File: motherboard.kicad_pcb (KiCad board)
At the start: 2 copper layers, 90.2 x 95.9 mm, 110 parts, among them P1 CONN_02X08, U1 STM32F411-LQFP64, U10 74LS125, U11 74LS125, U12 74LS125, U13 74LS125, U14 PCA9517A, U15 PCA9517A, U16 74LS125, U17 74LS125, U2 STM32F411-LQFP64, U3 AP7313, U4 74LS00, U5 74LS125, U6 FM25V20A-G, U7 FM25V20A-G, U8 FM25V20A-G, U9 FM25V20A-G, Y1 32k, Y2 8M(16pF), Y3 32k, Y4 8M(16pF)

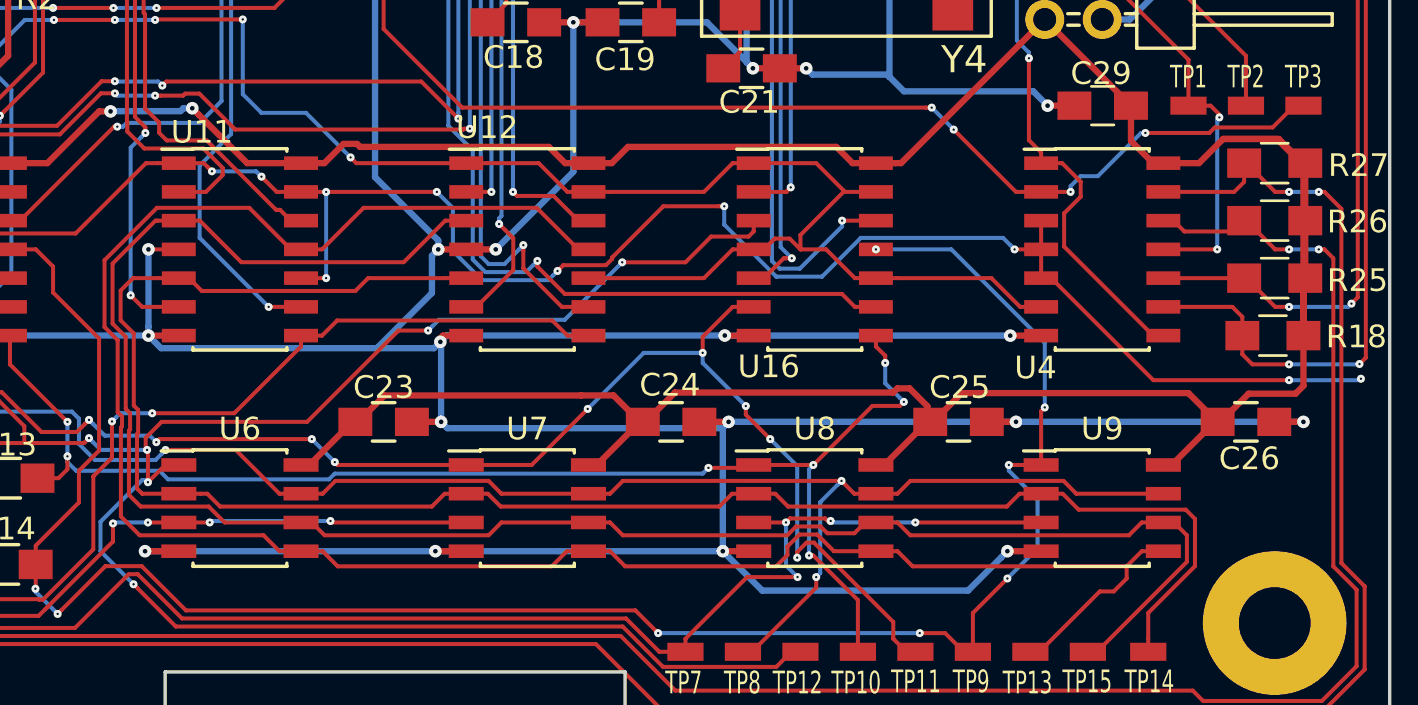
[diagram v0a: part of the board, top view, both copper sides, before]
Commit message: Adding ground plane
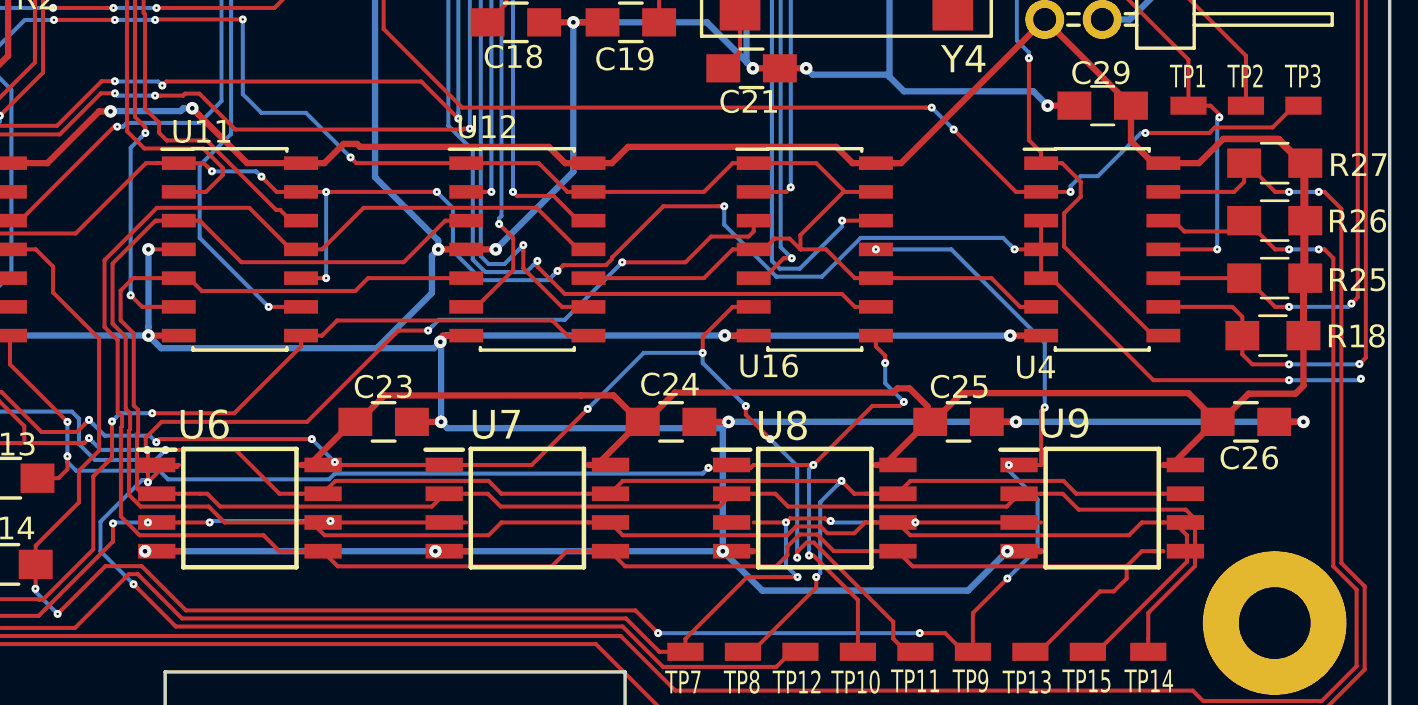
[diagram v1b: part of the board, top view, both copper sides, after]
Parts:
- U6, U7, U8, U9: footprint Housings_SOIC:SOIC-8_3.9x4.9mm_Pitch1.27mm -> FM25V20A-G:SOIC127P800X203-8N
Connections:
- C33 pad 1: /NBUFEN_SEC -> Net-(C33-Pad1)
- C33 pad 2: GND -> Net-(C33-Pad2)
- C35 pad 1: /NBUFEN_SEC -> Net-(C35-Pad1)
- C35 pad 2: GND -> Net-(C35-Pad2)
- R18 pad 2: +3V3 -> GND
- R25 pad 2: +3V3 -> GND
- R26 pad 2: +3V3 -> GND
- R27 pad 2: +3V3 -> GND
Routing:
- net /MEM_CS2: track 77.2 -> 49.7 mm, vias 9 -> 5
- net GND: track 752.4 -> 779.8 mm
- net /MEM_SCK: track 84.8 -> 111.2 mm, vias 0 -> 4
- net /MEM_NWP: track 113.3 -> 94.4 mm, vias 11 -> 7
- net /MEM_MISO: track 80.5 -> 73.1 mm
- net /NBUFEN_SEC: track 242.1 -> 235.4 mm
- net Net-(C35-Pad1): track 0.00 -> 5.90 mm
- net +3V3: track 584.4 -> 582.1 mm, vias 25 -> 29
- net Net-(C33-Pad2): track 0.00 -> 1.31 mm
- net Net-(C35-Pad2): track 0.00 -> 1.14 mm
- net Net-(C33-Pad1): track 0.00 -> 0.80 mm

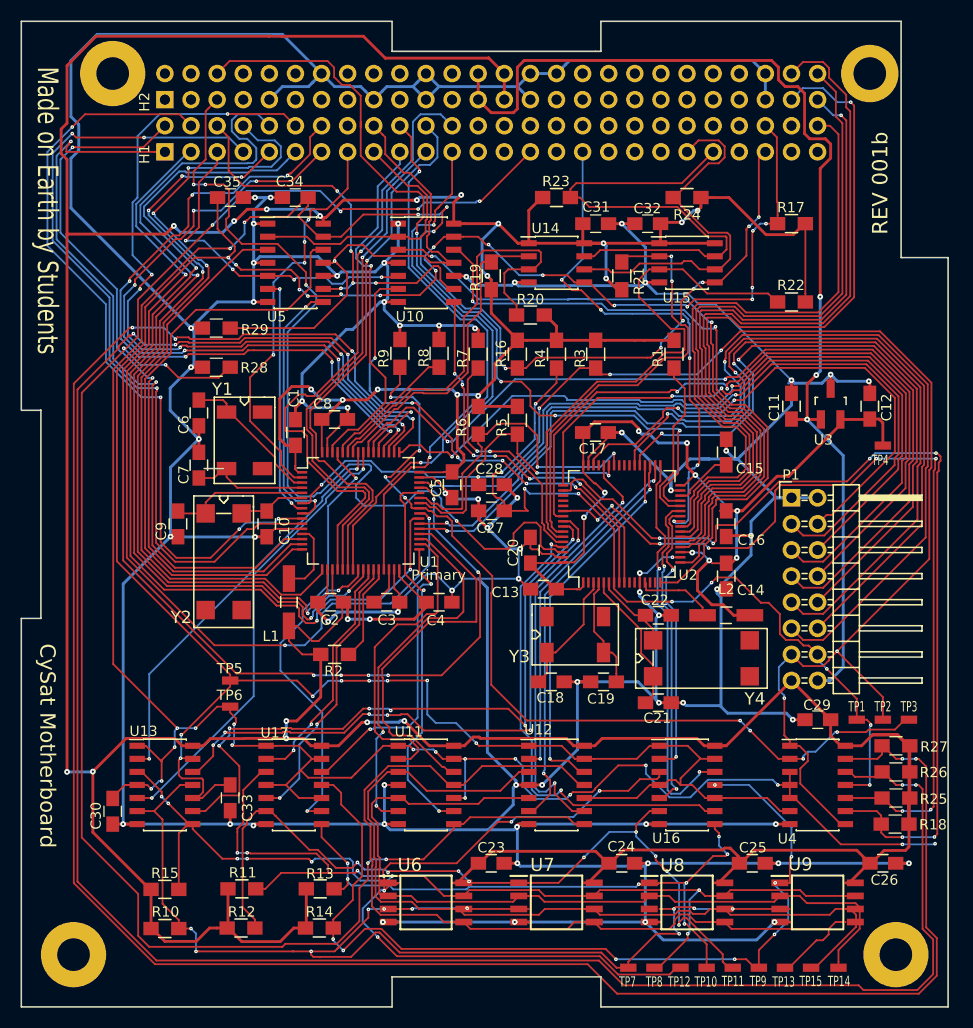
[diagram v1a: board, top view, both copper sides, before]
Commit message: Added ground plane and fixed footprints
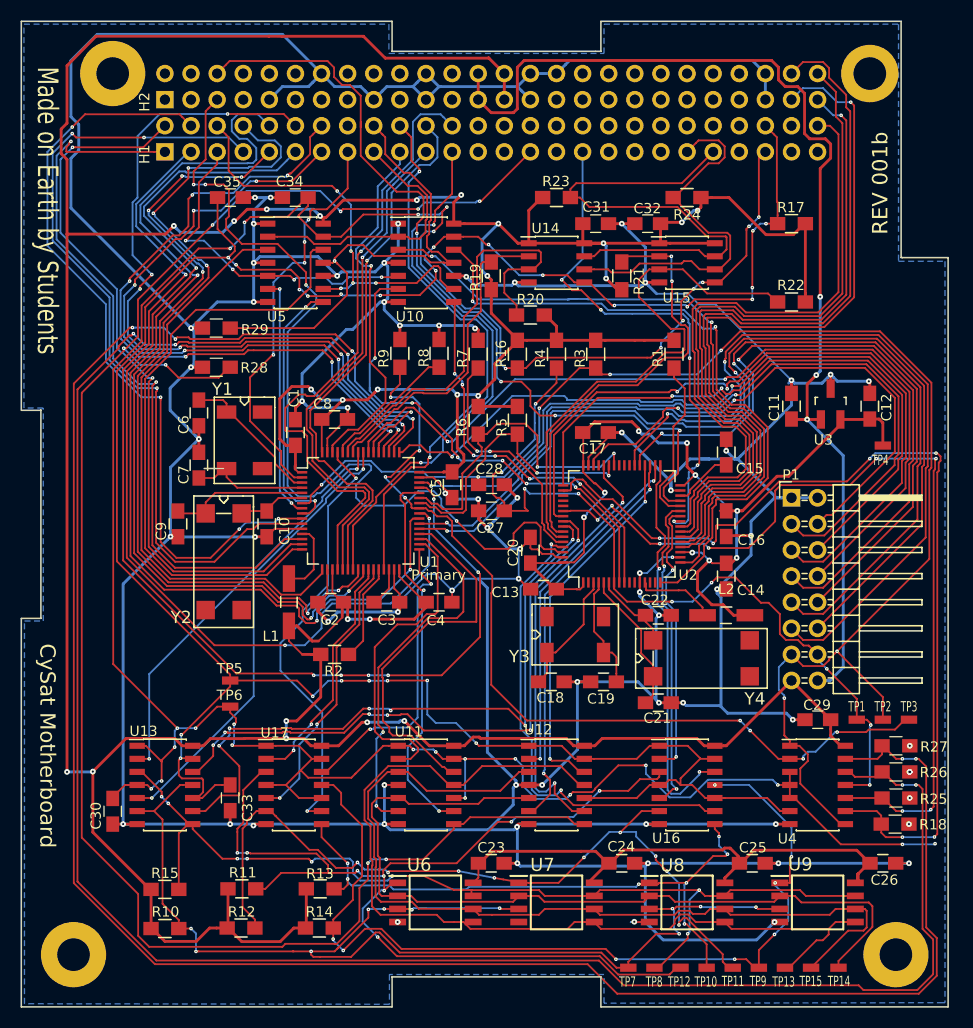
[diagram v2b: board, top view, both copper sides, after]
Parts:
- moved U6 0.91 mm to (153.3, 132.1)
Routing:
- net GND: track 779.8 -> 725.5 mm, vias 66 -> 70
- net +3V3: track 582.1 -> 549.7 mm, vias 29 -> 25
- net /MEM_CS2: track 49.7 -> 78.2 mm, vias 5 -> 9
- net /MEM_SCK: track 111.2 -> 87.1 mm, vias 4 -> 0
- net /MEM_NWP: track 94.4 -> 112.5 mm, vias 7 -> 11
- net /MEM_MISO: track 73.1 -> 82.3 mm
- net /MEM_CS1: track 60.2 -> 61.2 mm
- net /MEM_MOSI: track 92.4 -> 93.4 mm
- added copper zone on B.Cu, net GND

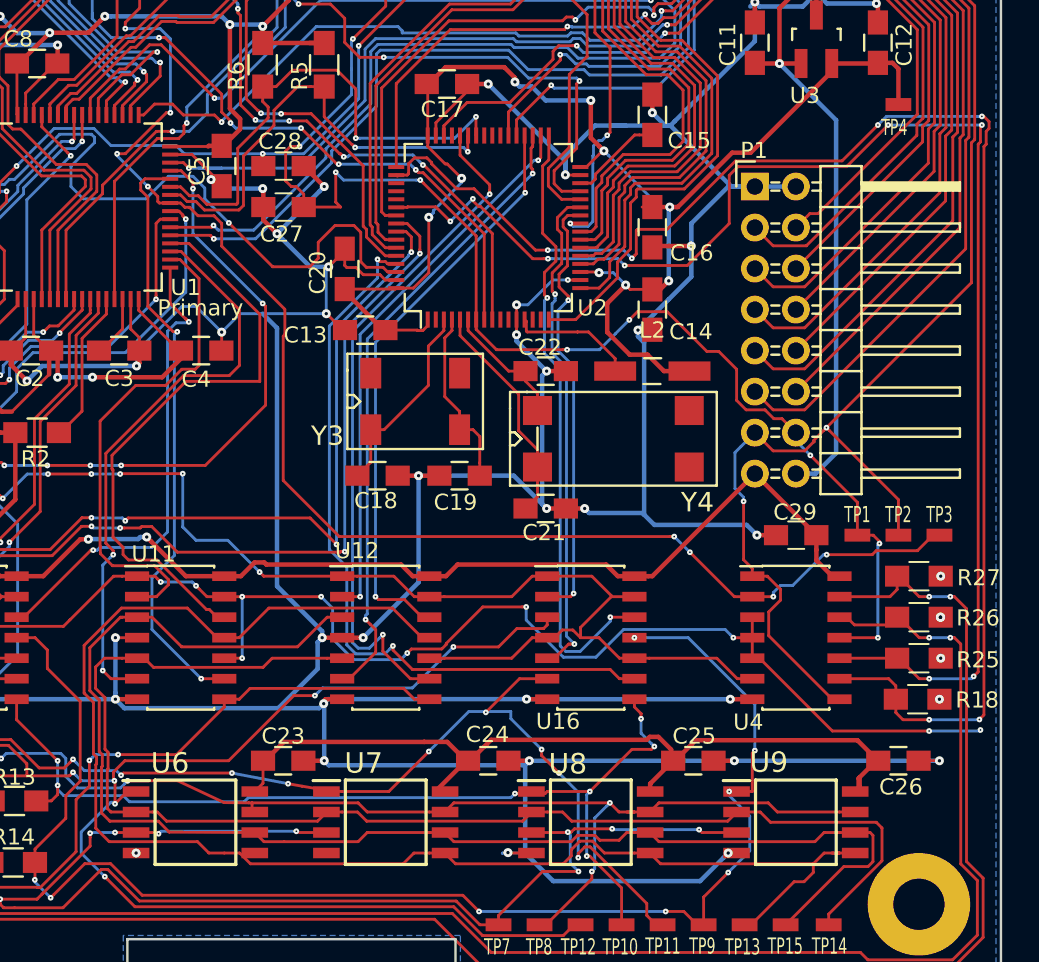
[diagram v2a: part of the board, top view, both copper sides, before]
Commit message: Added ground plane and fixed footprints
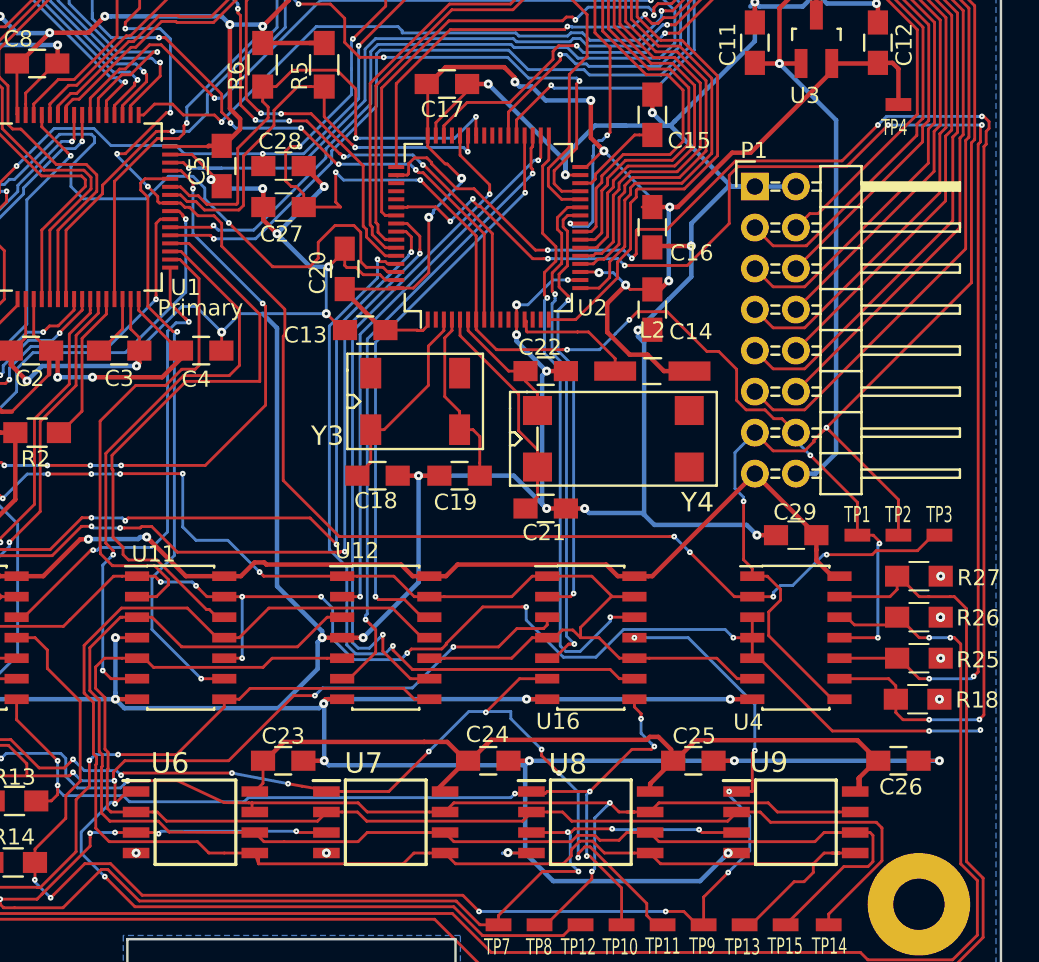
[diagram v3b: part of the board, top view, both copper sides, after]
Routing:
- net /MEM_MOSI: track 93.4 -> 94.4 mm
- net GND: vias 70 -> 71
- net /NRST2_S: vias 6 -> 4
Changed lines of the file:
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@@
   (general
     (links 392)
-    (no_connects 15)
+    (no_connects 13)
     (area 110.878219 46.279999 205.351781 142.315001)
     (thickness 1.6)
     (drawings 25)
-    (tracks 4148)
+    (tracks 4153)
     (zones 0)
     (modules 110)
@@
   (layers
     (0 F.Cu signal)
-    (31 B.Cu signal hide)
+    (31 B.Cu signal)
     (32 B.Adhes user hide)
     (33 F.Adhes user hide)
@@
       (effects (font (size 1 1) (thickness 0.15)))
     )
-    (pad 1 thru_hole circle (at 0 0) (size 6.35 6.35) (drill 3.175) (layers *.Mask B.Cu))
+    (pad 1 thru_hole circle (at 0 0) (size 6.35 6.35) (drill 3.175) (layers *.Cu *.Mask))
   )
   (module motherboard:Hole_0.125-0.250 locked (layer F.Cu)
@@
   (gr_line (start 149.098 139.319) (end 169.418 139.319) (layer Edge.Cuts) (width 0.15))
   (gr_line (start 149.098 142.24) (end 149.098 139.319) (layer Edge.Cuts) (width 0.15))
-  (via (at 199.47 116.84) (size 0.5588) (drill 0.2032) (layers F.Cu B.Cu) (net 1) (status C00000))
+  (via (at 161.425 133.985) (size 0.5588) (drill 0.2032) (layers F.Cu B.Cu) (net 1))
+  (segment (start 161.4424 134.0104) (end 161.4424 134.0024) (width 0.1778) (layer B.Cu) (net 1))
+  (segment (start 161.4424 134.0024) (end 161.425 133.985) (width 0.1778) (layer B.Cu) (net 1))
+  (via (at 199.47 116.84) (size 0.5588) (drill 0.2032) (layers F.Cu B.Cu) (net 1))
   (segment (start 199.37 116.84) (end 199.47 116.84) (width 0.2794) (layer F.Cu) (net 1))
-  (segment (start 199.47 116.84) (end 199.4408 116.84) (width 0.1778) (layer B.Cu) (net 1) (status 400000))
-  (via (at 199.47 119.38) (size 0.5588) (drill 0.2032) (layers F.Cu B.Cu) (net 1) (status C00000))
-  (segment (start 199.4408 119.38) (end 199.47 119.38) (width 0.1778) (layer F.Cu) (net 1) (status C00000))
-  (via (at 199.4408 119.38) (size 0.5588) (drill 0.2032) (layers F.Cu B.Cu) (net 1) (status 800000))
-  (segment (start 199.47 119.38) (end 199.4408 119.38) (width 0.1778) (layer B.Cu) (net 1) (status 400000))
-  (via (at 199.39 124.46) (size 0.5588) (drill 0.2032) (layers F.Cu B.Cu) (net 1) (status C00000))
-  (via (at 199.47 121.92) (size 0.5588) (drill 0.2032) (layers F.Cu B.Cu) (net 1) (status C00000))
+  (segment (start 199.47 116.84) (end 199.4408 116.84) (width 0.1778) (layer B.Cu) (net 1))
+  (via (at 199.47 119.38) (size 0.5588) (drill 0.2032) (layers F.Cu B.Cu) (net 1))
+  (segment (start 199.4408 119.38) (end 199.47 119.38) (width 0.1778) (layer F.Cu) (net 1))
+  (via (at 199.4408 119.38) (size 0.5588) (drill 0.2032) (layers F.Cu B.Cu) (net 1))
+  (segment (start 199.47 119.38) (end 199.4408 119.38) (width 0.1778) (layer B.Cu) (net 1))
+  (via (at 199.39 124.46) (size 0.5588) (drill 0.2032) (layers F.Cu B.Cu) (net 1))
+  (via (at 199.47 121.92) (size 0.5588) (drill 0.2032) (layers F.Cu B.Cu) (net 1))
   (segment (start 199.39 122) (end 199.47 121.92) (width 0.2794) (layer F.Cu) (net 1))
-  (segment (start 199.47 121.92) (end 199.4408 121.92) (width 0.1778) (layer B.Cu) (net 1) (status 400000))
-  (segment (start 199.3392 128.27) (end 198.1 128.27) (width 0.1778) (layer F.Cu) (net 1) (status 800000))
-  (segment (start 174.125 133.985) (end 172.6946 133.985) (width 0.1778) (layer F.Cu) (net 1) (status 400000))
+  (segment (start 199.47 121.92) (end 199.4408 121.92) (width 0.1778) (layer B.Cu) (net 1))
+  (segment (start 199.3392 128.27) (end 198.1 128.27) (width 0.1778) (layer F.Cu) (net 1))
+  (segment (start 174.125 133.985) (end 172.6946 133.985) (width 0.1778) (layer F.Cu) (net 1))
   (via (at 172.6692 133.9596) (size 0.5588) (drill 0.2032) (layers F.Cu B.Cu) (net 1))
   (segment (start 172.6946 133.985) (end 172.6692 133.9596) (width 0.1778) (layer F.Cu) (net 1))
@@
   (segment (start 172.6692 133.985) (end 172.339 133.985) (width 0.1778) (layer B.Cu) (net 1))
   (segment (start 172.339 133.985) (end 172.3136 134.0104) (width 0.1778) (layer B.Cu) (net 1))
-  (via (at 149.6394 133.985) (size 0.5588) (drill 0.2032) (layers F.Cu B.Cu) (net 1) (status C00000))
+  (via (at 149.6394 133.985) (size 0.5588) (drill 0.2032) (layers F.Cu B.Cu) (net 1))
   (segment (start 149.2504 134.0104) (end 149.2584 134.0024) (width 0.1778) (layer B.Cu) (net 1))
   (segment (start 149.6568 134.0024) (end 149.2584 134.0024) (width 0.1778) (layer B.Cu) (net 1))
-  (segment (start 149.6568 134.0024) (end 149.6394 133.985) (width 0.1778) (layer B.Cu) (net 1) (status 800000))
+  (segment (start 149.6568 134.0024) (end 149.6394 133.985) (width 0.1778) (layer B.Cu) (net 1))
   (segment (start 185.42 128.3208) (end 186.6392 128.3208) (width 0.1778) (layer B.Cu) (net 1))
   (segment (start 186.6392 128.3208) (end 186.69 128.27) (width 0.1778) (layer B.Cu) (net 1))
@@
   (segment (start 193.675 131.445) (end 193.2 131.445) (width 0.1778) (layer F.Cu) (net 61))
   (segment (start 180.025 131.445) (end 180.5 131.445) (width 0.1778) (layer F.Cu) (net 61))
+  (segment (start 157.226 134.653301) (end 157.226 134.2216) (width 0.1778) (layer F.Cu) (net 62))
+  (segment (start 157.226 134.2216) (end 156.9894 133.985) (width 0.1778) (layer F.Cu) (net 62))
   (segment (start 193.1416 133.985) (end 194.175 133.985) (width 0.1778) (layer F.Cu) (net 62))
   (segment (start 147.973063 133.281701) (end 153.443901 133.281701) (width 0.1778) (layer F.Cu) (net 62))
@@
   (segment (start 169.421101 134.653301) (end 168.7528 133.985) (width 0.1778) (layer F.Cu) (net 62))
   (segment (start 168.7528 133.985) (end 167.8 133.985) (width 0.1778) (layer F.Cu) (net 62))
-  (segment (start 156.0528 133.985) (end 155.1 133.985) (width 0.1778) (layer F.Cu) (net 62))
-  (segment (start 156.721101 134.653301) (end 156.0528 133.985) (width 0.1778) (layer F.Cu) (net 62))
-  (segment (start 166.178899 134.653301) (end 156.721101 134.653301) (width 0.1778) (layer F.Cu) (net 62))
+  (segment (start 156.9894 133.985) (end 155.1 133.985) (width 0.1778) (layer F.Cu) (net 62))
+  (segment (start 156.9894 133.985) (end 156.9894 133.985) (width 0.1778) (layer F.Cu) (net 62))
+  (segment (start 166.178899 134.653301) (end 157.226 134.653301) (width 0.1778) (layer F.Cu) (net 62))
+  (segment (start 157.226 134.653301) (end 156.9894 133.985) (width 0.1778) (layer F.Cu) (net 62))
   (segment (start 166.8472 133.985) (end 166.178899 134.653301) (width 0.1778) (layer F.Cu) (net 62))
   (segment (start 167.8 133.985) (end 166.8472 133.985) (width 0.1778) (layer F.Cu) (net 62))
@@
   (segment (start 197.04561 119.527298) (end 197.04561 119.38) (width 0.1778) (layer F.Cu) (net 156))
   (segment (start 196.69 119.38) (end 196.59 119.38) (width 0.1778) (layer F.Cu) (net 156))
-  (segment (start 126.896611 76.150931) (end 124.089179 76.150931) (width 0.1778) (layer B.Cu) (net 157))
+  (segment (start 198.7296 118.11) (end 200.06691 118.11) (width 0.1778) (layer F.Cu) (net 157))
   (segment (start 123.586285 76.150931) (end 123.837732 76.150931) (width 0.1778) (layer F.Cu) (net 157))
   (segment (start 118.135389 81.601827) (end 123.586285 76.150931) (width 0.1778) (layer F.Cu) (net 157))
@@
   (segment (start 149.293062 85.788498) (end 150.704051 84.377509) (width 0.1778) (layer F.Cu) (net 157))
   (segment (start 148.757638 85.788498) (end 149.293062 85.788498) (width 0.1778) (layer F.Cu) (net 157))
-  (segment (start 147.3 88.28) (end 147.3 87.246136) (width 0.1778) (layer F.Cu) (net 157))
+  (segment (start 147.3 87.246136) (end 147.3 88.28) (width 0.1778) (layer F.Cu) (net 157))
   (via (at 145.221118 78.436806) (size 0.3556) (drill 0.1016) (layers F.Cu B.Cu) (net 157))
   (via (at 150.955498 84.377509) (size 0.3556) (drill 0.1016) (layers F.Cu B.Cu) (net 157))
-  (segment (start 198.755 118.11) (end 200.06691 118.11) (width 0.1778) (layer B.Cu) (net 157))
-  (via (at 200.06691 118.11) (size 0.3556) (drill 0.1016) (layers F.Cu B.Cu) (net 157))
-  (segment (start 196.77 116.84) (end 196.87 116.84) (width 0.1778) (layer F.Cu) (net 157))
+  (segment (start 126.896611 76.150931) (end 124.089179 76.150931) (width 0.1778) (layer B.Cu) (net 157))
+  (segment (start 198.14 118.11) (end 198.7296 118.11) (width 0.1778) (layer F.Cu) (net 157))
+  (segment (start 198.7296 118.11) (end 198.755 118.11) (width 0.1778) (layer F.Cu) (net 157))
   (segment (start 196.87 116.84) (end 198.14 118.11) (width 0.1778) (layer F.Cu) (net 157))
-  (segment (start 198.14 118.11) (end 198.755 118.11) (width 0.1778) (layer F.Cu) (net 157))
-  (via (at 198.755 118.11) (size 0.3556) (drill 0.1016) (layers F.Cu B.Cu) (net 157))
+  (segment (start 196.77 116.84) (end 196.87 116.84) (width 0.1778) (layer F.Cu) (net 157))
   (segment (start 193.2 118.11) (end 196.3278 118.11) (width 0.1778) (layer F.Cu) (net 157))
   (segment (start 196.3278 118.11) (end 196.77 117.6678) (width 0.1778) (layer F.Cu) (net 157))
